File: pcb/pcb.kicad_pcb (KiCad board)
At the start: 2 copper layers, 61 x 81 mm, 46 parts, among them J1 LEFT, J2 LEFT-EXT, J3 RIGHT, J4 RIGHT-EXT, J5 EXT POWER, J6 RJ45, J7 RJ45, SW1 Reset, SW2 Factory Reset, SW3 User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

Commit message: :pencil: Initial pass at firmware and updates to the PCB.
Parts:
- added C13: 100nF, Capacitor_SMD:C_0603_1608Metric, F.Cu at (112.7, 108.1)
- D3: value CAN RX -> CAN TX
- D4: value CAN TX -> CAN RX
- moved JP1 15.1 mm to (159.7, 108.6), turned to 180 degrees
- moved J5 12.6 mm to (158.7, 120.0)
- moved U4 6.08 mm to (116.2, 110.3), turned to 90 degrees
- moved D4 3.42 mm to (111.2, 111.2), turned to 270 degrees
- moved R8 3.14 mm to (112.7, 111.2), turned to 90 degrees
- moved D3 2.68 mm to (111.2, 114.2), turned to 90 degrees
- moved R7 2.31 mm to (112.7, 114.2), turned to 270 degrees
- moved U2 2.02 mm to (140.9, 104.0)
- moved C1 1.89 mm to (145.6, 103.0)
- moved C11 1.78 mm to (117.3, 105.7)
- moved U5 1.70 mm to (122.7, 107.7)
- moved C12 1.70 mm to (128.3, 107.1)
- moved D5 1.17 mm to (117.6, 116.7)
- moved C3 1.12 mm to (136.5, 107.1)
- moved C4 1.12 mm to (133.5, 107.1)
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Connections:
- U4 pad 3: CAN-RX -> CAN-TX
- U4 pad 5: CAN-TX -> CAN-RX
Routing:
- net +3V3: track 187.0 -> 200.7 mm, vias 1 -> 6
- net VCC: track 24.0 -> 34.4 mm
- net Net-(R7-Pad1): track 13.4 -> 3.09 mm, vias 2 -> 0
- net VDDA: track 23.0 -> 32.9 mm
- net VDD: track 16.1 -> 8.95 mm
- net +5V: track 50.0 -> 43.3 mm, vias 0 -> 1
- net CAN-RX: track 58.1 -> 52.6 mm
- net CAN-H: track 38.3 -> 33.1 mm, vias 0 -> 1
- net CAN-TX: track 66.4 -> 61.6 mm
- net Net-(R8-Pad1): track 3.54 -> 6.74 mm
- net CAN-L: track 35.8 -> 33.7 mm, vias 0 -> 1
- net RESET: track 49.2 -> 47.4 mm
- net /5V-BST: track 1.55 -> 2.60 mm
- net Net-(C2-Pad1): track 8.61 -> 9.67 mm
- net ALT-B: track 19.1 -> 20.1 mm
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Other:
- board text added: "CAN"
- board text added: "Remove JP1 to use USB"
- board text added: "WARNING"
- board text added: "v1.0 Nov 2020"
- board text removed: "!WARNING!"
- board text removed: "CAN Activity"
- board text removed: "Remove JP1 when using USB"

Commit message: :pencil: Corrections to part numbers
* C2 should have been 100nF and not 22uF
* U3 needs to be able to provide 1A and not 600mA.
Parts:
- C2: value 22uF -> 100nF
- U3: value NCP1117 -> AP2114-3.3

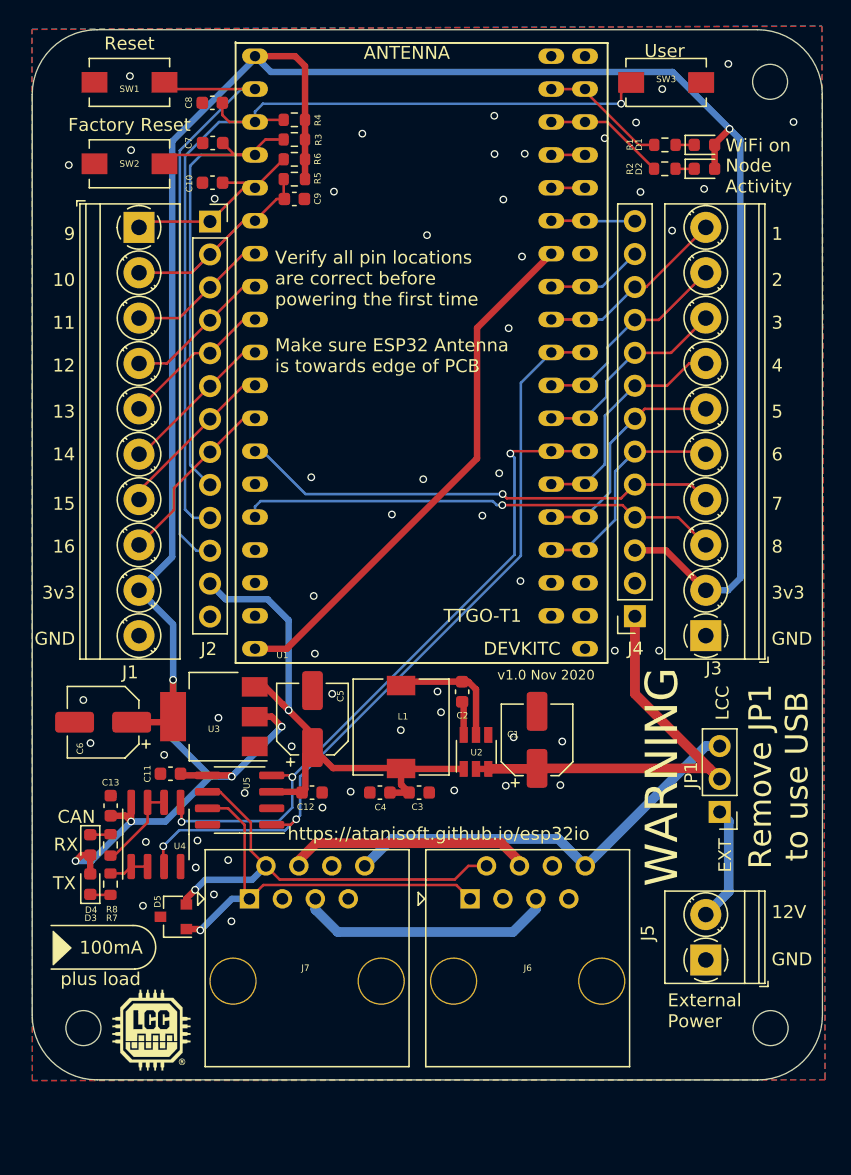
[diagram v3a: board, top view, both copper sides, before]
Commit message: :pencil: Add Fiducials to PCB :pencil: Adjust LED colors so they are not all red
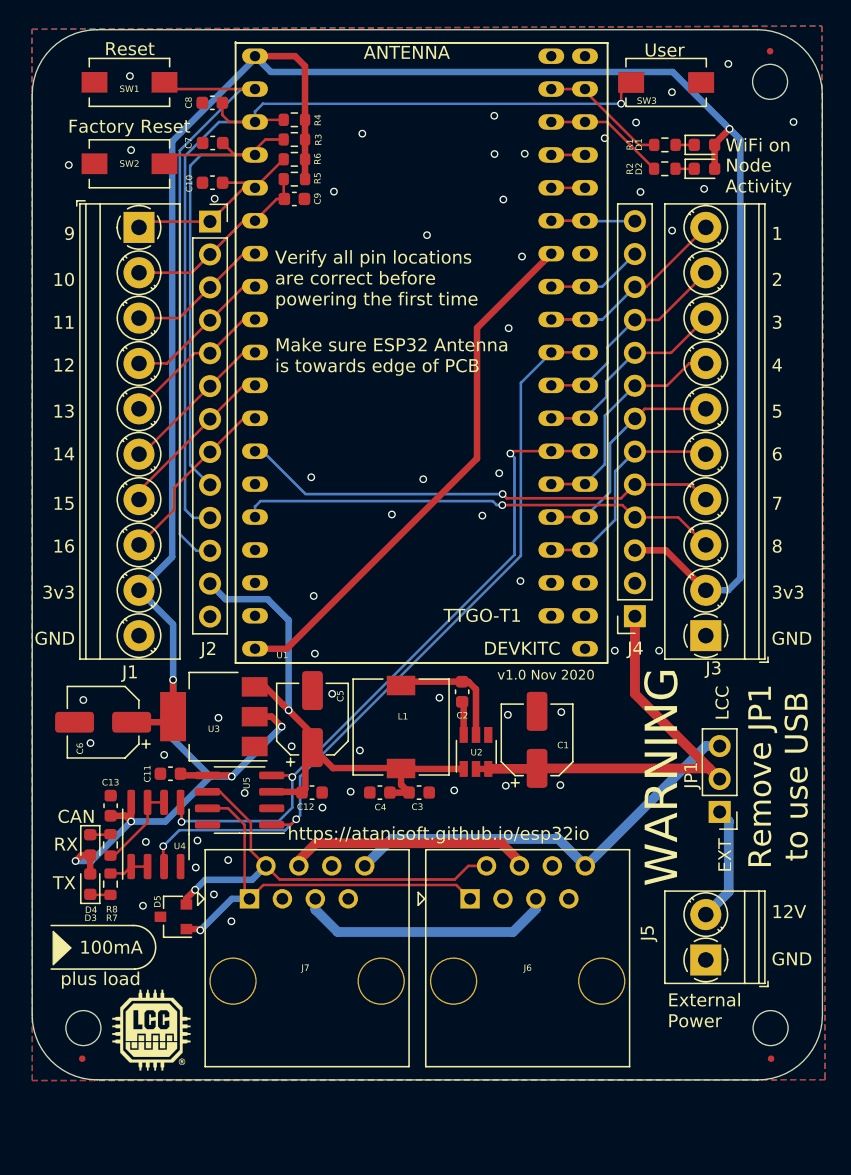
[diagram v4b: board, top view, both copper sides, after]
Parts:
- added FID1: Fiducial, Fiducial:Fiducial_0.5mm_Mask1mm, F.Cu at (163.6, 49.9)
- added FID2: Fiducial, Fiducial:Fiducial_0.5mm_Mask1mm, F.Cu at (110.5, 127.7)
- added FID3: Fiducial, Fiducial:Fiducial_0.5mm_Mask1mm, F.Cu at (163.7, 127.7)
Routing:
- net GND: vias 55 -> 54
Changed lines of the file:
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@@
     (thickness 1.6)
     (drawings 53)
-    (tracks 395)
+    (tracks 394)
     (zones 0)
-    (modules 47)
+    (modules 50)
     (nets 47)
   )
@@
   (title_block
     (title "ESP32 IO Board")
-    (date 2020-11-16)
+    (date 2020-11-19)
     (rev 1.0)
   )
@@
     (add_net VDDA)
     (add_net WIFI_LED)
+  )
+  (module Fiducial:Fiducial_0.5mm_Mask1mm (layer F.Cu)
+    (at 163.69 127.65)
+    (descr "Circular Fiducial, 0.5mm bare copper, 1mm soldermask opening (Level C)")
+    (tags fiducial)
+    (attr smd)
+    (fp_text reference FID3 (at 0 -1.5) (layer F.SilkS) hide
+      (effects (font (size 1 1) (thickness 0.15)))
+    )
+    (fp_text value Fiducial (at 0 1.5) (layer F.Fab)
+      (effects (font (size 1 1) (thickness 0.15)))
+    )
+    (fp_circle (center 0 0) (end 0.5 0) (layer F.Fab) (width 0.1))
+    (fp_circle (center 0 0) (end 0.75 0) (layer F.CrtYd) (width 0.05))
+    (fp_text user %R (at 0 0) (layer F.Fab)
+      (effects (font (size 0.2 0.2) (thickness 0.04)))
+    )
+    (pad "" smd circle (at 0 0) (size 0.5 0.5) (layers F.Cu F.Mask)
+      (solder_mask_margin 0.25) (clearance 0.25))
+  )
+  (module Fiducial:Fiducial_0.5mm_Mask1mm (layer F.Cu)
+    (at 110.54 127.65)
+    (descr "Circular Fiducial, 0.5mm bare copper, 1mm soldermask opening (Level C)")
+    (tags fiducial)
+    (attr smd)
+    (fp_text reference FID2 (at 0 -1.5) (layer F.SilkS) hide
+      (effects (font (size 1 1) (thickness 0.15)))
+    )
+    (fp_text value Fiducial (at 0 1.5) (layer F.Fab)
+      (effects (font (size 1 1) (thickness 0.15)))
+    )
+    (fp_circle (center 0 0) (end 0.5 0) (layer F.Fab) (width 0.1))
+    (fp_circle (center 0 0) (end 0.75 0) (layer F.CrtYd) (width 0.05))
+    (fp_text user %R (at 0 0) (layer F.Fab)
+      (effects (font (size 0.2 0.2) (thickness 0.04)))
+    )
+    (pad "" smd circle (at 0 0) (size 0.5 0.5) (layers F.Cu F.Mask)
+      (solder_mask_margin 0.25) (clearance 0.25))
+  )
+  (module Fiducial:Fiducial_0.5mm_Mask1mm (layer F.Cu)
+    (at 163.61 49.92)
+    (descr "Circular Fiducial, 0.5mm bare copper, 1mm soldermask opening (Level C)")
+    (tags fiducial)
+    (attr smd)
+    (fp_text reference FID1 (at 0 -1.5) (layer F.SilkS) hide
+      (effects (font (size 1 1) (thickness 0.15)))
+    )
+    (fp_text value Fiducial (at 0 1.5) (layer F.Fab)
+      (effects (font (size 1 1) (thickness 0.15)))
+    )
+    (fp_circle (center 0 0) (end 0.5 0) (layer F.Fab) (width 0.1))
+    (fp_circle (center 0 0) (end 0.75 0) (layer F.CrtYd) (width 0.05))
+    (fp_text user %R (at 0 0) (layer F.Fab)
+      (effects (font (size 0.2 0.2) (thickness 0.04)))
+    )
+    (pad "" smd circle (at 0 0) (size 0.5 0.5) (layers F.Cu F.Mask)
+      (solder_mask_margin 0.25) (clearance 0.25))
   )
   (module Connector_PinHeader_2.54mm:PinHeader_1x03_P2.54mm_Vertical (layer F.Cu)
@@
     (descr "Light Touch Switch, https://industrial.panasonic.com/cdbs/www-data/pdf/ATK0000/ATK0000CE7.pdf")
     (attr smd)
-    (fp_text reference SW3 (at 0 -0.254) (layer F.SilkS)
-      (effects (font (size 0.5 0.5) (thickness 0.1)))
-    )
-    (fp_text value User (at -0.12 -2.43) (layer F.SilkS)
+    (fp_text reference SW3 (at -1.49 1.42) (layer F.SilkS)
+      (effects (font (size 0.5 0.5) (thickness 0.1)))
+    )
+    (fp_text value User (at -0.13 -2.47) (layer F.SilkS)
       (effects (font (size 1 1) (thickness 0.15)))
     )
@@
       (effects (font (size 0.5 0.5) (thickness 0.1)))
     )
-    (fp_text value "Factory Reset" (at 0 3) (layer F.SilkS)
+    (fp_text value "Factory Reset" (at 0.012 2.864) (layer F.SilkS)
       (effects (font (size 1 1) (thickness 0.15)))
     )
@@
       (effects (font (size 0.5 0.5) (thickness 0.1)))
     )
-    (fp_text value Reset (at 0 3) (layer F.SilkS)
+    (fp_text value Reset (at -0.018 2.564) (layer F.SilkS)
       (effects (font (size 1 1) (thickness 0.15)))
     )
@@
     (tags "capacitor electrolytic")
     (attr smd)
-    (fp_text reference C1 (at 0.42 -1.85 180) (layer F.SilkS)
+    (fp_text reference C1 (at -0.42 2.01 180) (layer F.SilkS)
       (effects (font (size 0.5 0.5) (thickness 0.1)))
     )
@@
   (via (at 115.225 115.85) (size 0.6) (drill 0.4) (layers F.Cu B.Cu) (net 1))
   (via (at 122.05 117.05) (size 0.6) (drill 0.4) (layers F.Cu B.Cu) (net 1))
-  (via (at 155.29 52.84) (size 0.6) (drill 0.4) (layers F.Cu B.Cu) (net 1))
+  (via (at 156.04 53.08) (size 0.6) (drill 0.4) (layers F.Cu B.Cu) (net 1))
   (via (at 129.96 60.75) (size 0.6) (drill 0.4) (layers F.Cu B.Cu) (net 1))
   (via (at 109.5 58.7) (size 0.6) (drill 0.4) (layers F.Cu B.Cu) (net 1))
@@
   (via (at 128.21 82.79) (size 0.6) (drill 0.4) (layers F.Cu B.Cu) (net 1))
   (via (at 144.35 90.8) (size 0.6) (drill 0.4) (layers F.Cu B.Cu) (net 1))
-  (via (at 135.12 102.3) (size 0.6) (drill 0.4) (layers F.Cu B.Cu) (net 1))
+  (via (at 131.96 103.87) (size 0.6) (drill 0.4) (layers F.Cu B.Cu) (net 1))
   (via (at 158.52 60.54) (size 0.6) (drill 0.4) (layers F.Cu B.Cu) (net 1))
   (via (at 165.42 55.38) (size 0.6) (drill 0.4) (layers F.Cu B.Cu) (net 1))
@@
   (via (at 121.05 101.35) (size 0.6) (drill 0.4) (layers F.Cu B.Cu) (net 1))
   (via (at 111.175 103.3) (size 0.6) (drill 0.4) (layers F.Cu B.Cu) (net 1))
-  (via (at 147.575 103.175) (size 0.6) (drill 0.4) (layers F.Cu B.Cu) (net 1))
+  (via (at 147.5 100.91) (size 0.6) (drill 0.4) (layers F.Cu B.Cu) (net 1))
   (via (at 139.24 106.95) (size 0.6) (drill 0.4) (layers F.Cu B.Cu) (net 1))
   (via (at 129.825 99.5) (size 0.6) (drill 0.4) (layers F.Cu B.Cu) (net 1))
-  (via (at 138.22 100.92) (size 0.6) (drill 0.4) (layers F.Cu B.Cu) (net 1))
+  (via (at 138.1 99.8) (size 0.6) (drill 0.4) (layers F.Cu B.Cu) (net 1))
   (via (at 143.22 106.59) (size 0.6) (drill 0.4) (layers F.Cu B.Cu) (net 1))
-  (via (at 143.825 102.85) (size 0.6) (drill 0.4) (layers F.Cu B.Cu) (net 1))
+  (via (at 143.38 101.12) (size 0.6) (drill 0.4) (layers F.Cu B.Cu) (net 1))
   (via (at 110.625 99.975) (size 0.6) (drill 0.4) (layers F.Cu B.Cu) (net 1))
   (via (at 134.43 85.66) (size 0.6) (drill 0.4) (layers F.Cu B.Cu) (net 1))
@@
   (via (at 114.31 57.55) (size 0.6) (drill 0.4) (layers F.Cu B.Cu) (net 1))
   (via (at 120.76 61.3) (size 0.6) (drill 0.4) (layers F.Cu B.Cu) (net 1))
-  (via (at 137.95 99.32) (size 0.6) (drill 0.4) (layers F.Cu B.Cu) (net 1))
   (via (at 147.43 106.54) (size 0.6) (drill 0.4) (layers F.Cu B.Cu) (net 1))
   (via (at 131.25 107.05) (size 0.6) (drill 0.4) (layers F.Cu B.Cu) (net 1))

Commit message: pcb update for rename of repo
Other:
- board text added: "https://atanisoft.github.io/esp32olcbio"

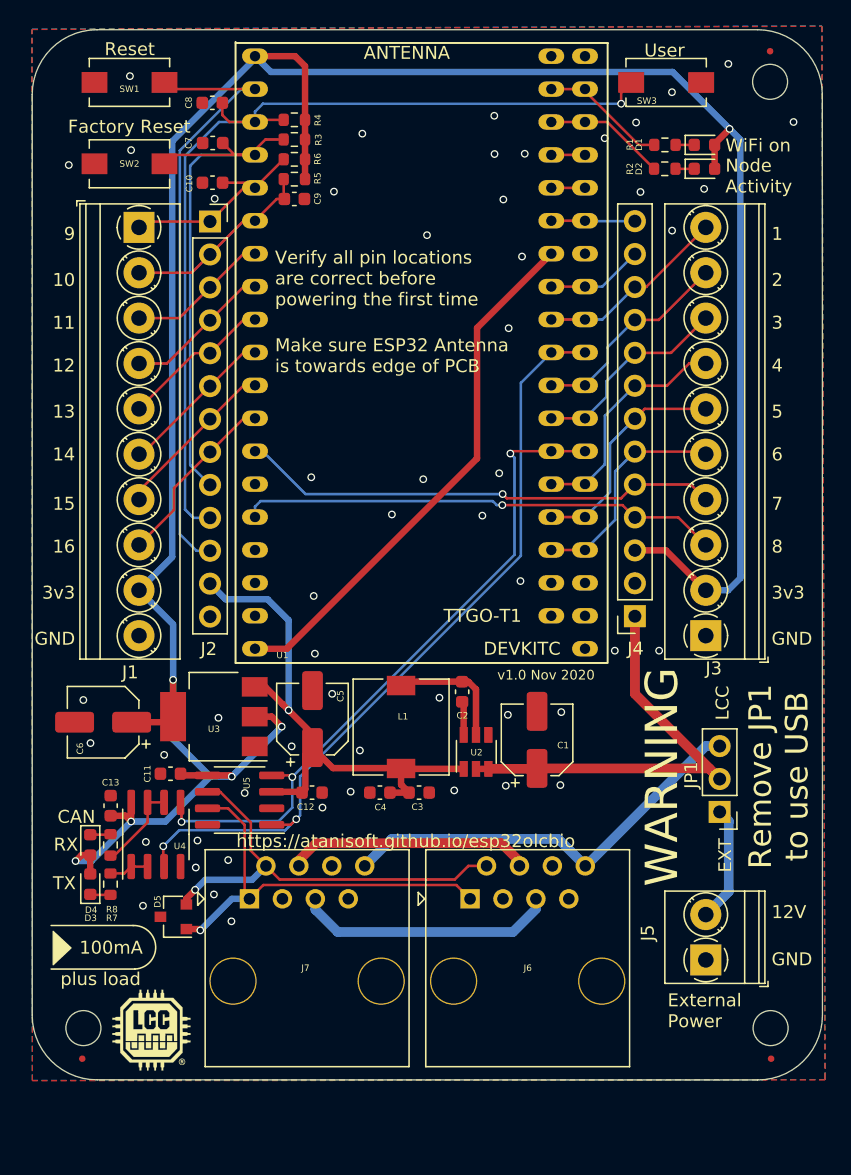
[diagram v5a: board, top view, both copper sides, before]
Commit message: PCB updates for KiCad6
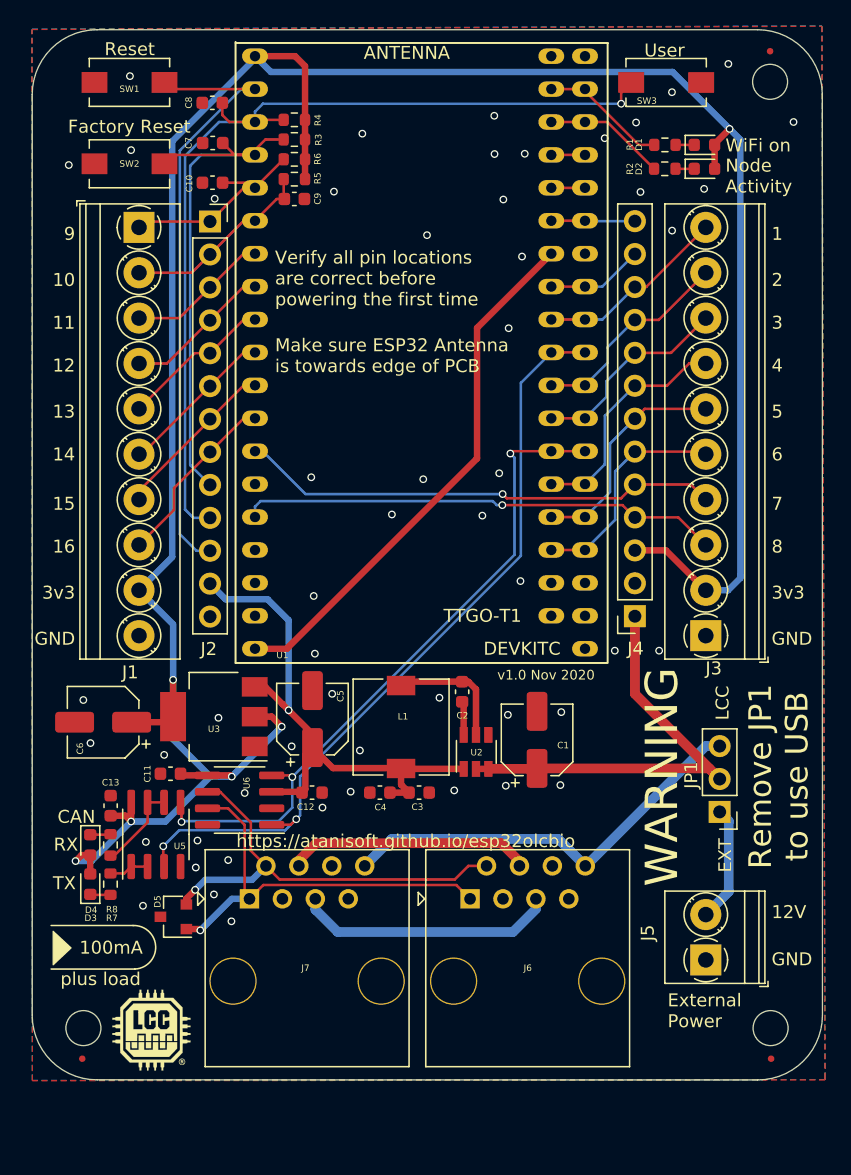
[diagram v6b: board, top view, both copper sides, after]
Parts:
- renumbered U4 to U5, U5 to U6
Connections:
- U1 pad 1: Net-(U1-Pad1) -> unconnected-(U1-Pad1)
- U1 pad 3: Net-(U1-Pad3) -> unconnected-(U1-Pad3)
- U1 pad 5V: Net-(U1-Pad5V) -> unconnected-(U1-Pad5V)
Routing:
- net unconnected-(U1-Pad5V): track 0.00 -> 41.4 mm
- net Net-(U1-Pad5V): track 41.4 -> 0.00 mm
- net unconnected-(U1-Pad3): track 0.00 -> 2.60 mm
- net unconnected-(U1-Pad1): track 0.00 -> 2.60 mm
- net Net-(U1-Pad3): track 2.60 -> 0.00 mm
- net Net-(U1-Pad1): track 2.60 -> 0.00 mm
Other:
- net class Default removed

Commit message: IO PCB v1.1
Spaced out RJ45 jacks to provide easier access to USB connector.

Fixes: https://github.com/atanisoft/Esp32OlcbIO/issues/3
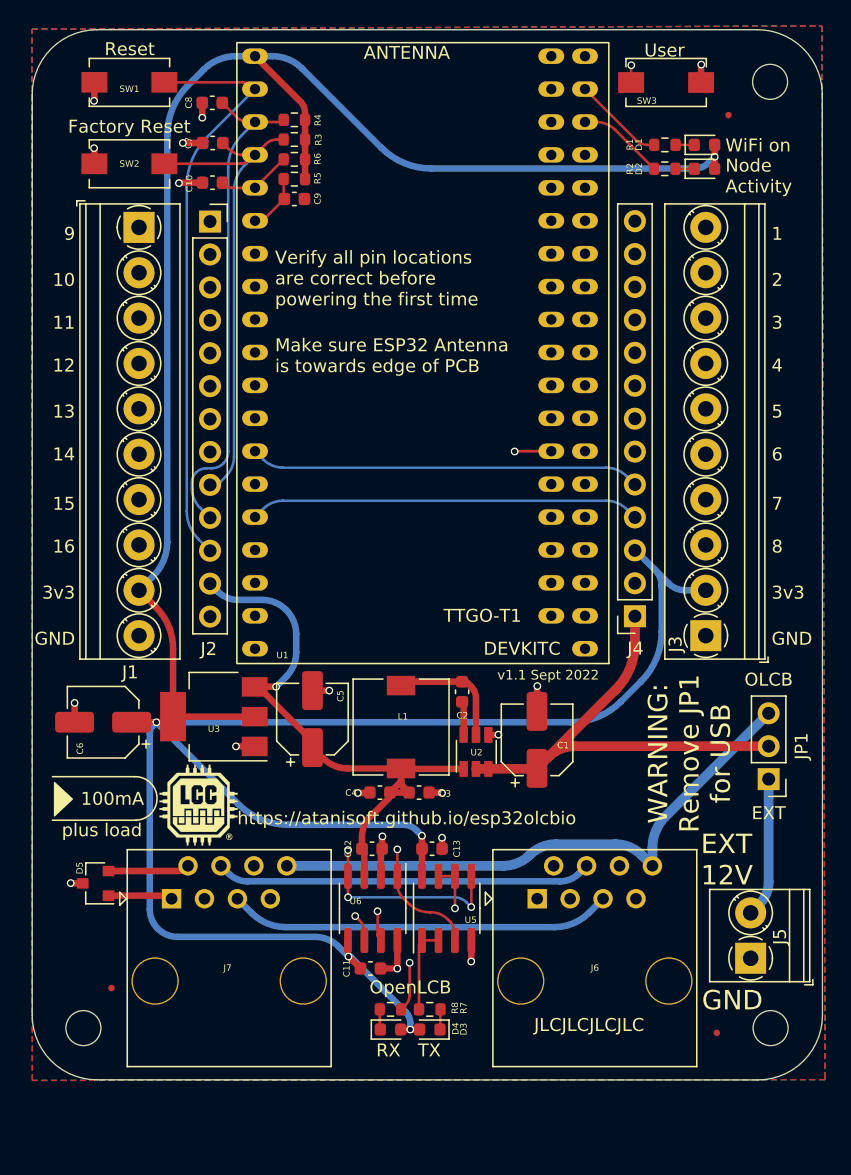
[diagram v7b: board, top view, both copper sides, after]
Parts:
- added REF**: OSHW-Logo2_7.3x6mm_SilkScreen, Symbol:OSHW-Logo2_7.3x6mm_SilkScreen, B.Cu at (136.9, 64.8)
- added REF**: KiCad-Logo2_5mm_SilkScreen, Symbol:KiCad-Logo2_5mm_SilkScreen, B.Cu at (137.0, 58.6)
- moved D3 28.5 mm to (137.4, 125.4), turned to 180 degrees
- moved D4 27.2 mm to (134.3, 125.4), turned to 0 degrees
- moved R7 26.5 mm to (137.4, 123.8), turned to 0 degrees
- moved R8 25.1 mm to (134.3, 123.8), turned to 180 degrees
- moved C13 25.0 mm to (137.5, 111.5), turned to 180 degrees
- moved U5 23.2 mm to (138.7, 116.0)
- moved C11 21.5 mm to (132.8, 120.7), turned to 0 degrees
- moved G*** 17.7 mm to (119.5, 108.0)
- moved U6 13.2 mm to (132.9, 116.0), turned to -90 degrees
- moved D5 6.54 mm to (111.6, 114.1)
- moved C12 6.34 mm to (132.9, 111.5)
- moved J7 6.01 mm to (117.4, 115.3)
- moved FID2 5.90 mm to (112.8, 122.2)
- moved FID1 5.88 mm to (160.4, 54.9)
- moved J6 5.18 mm to (145.6, 115.3)
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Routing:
- net +3V3: track 200.7 -> 243.9 mm, vias 6 -> 5
- net unconnected-(U1-Pad5V): track 41.4 -> 0.00 mm
- net GND: track 0.00 -> 27.5 mm, vias 54 -> 18
- net VDDA: track 32.9 -> 44.5 mm
- net ALT-A: track 18.9 -> 29.0 mm
- net ALT-B: track 20.1 -> 29.7 mm
- net CAN-L: track 33.7 -> 41.5 mm
- net CAN-TX: track 61.6 -> 54.8 mm, vias 2 -> 1
- net Net-(R8-Pad1): track 6.74 -> 13.2 mm, vias 0 -> 2
- net CAN-RX: track 52.6 -> 57.0 mm, vias 3 -> 4
- net CAN-H: track 33.1 -> 37.3 mm
- net FACTORY_RESET: track 43.7 -> 39.6 mm
- net Net-(R7-Pad1): track 3.09 -> 6.65 mm
- net VCC: track 34.4 -> 37.7 mm
- net +5V: track 43.3 -> 46.1 mm
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- added copper zone on In1.Cu, net GND
- added copper zone on In2.Cu, net GND
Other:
- copper layers 2 -> 4
- board text added: "EXT 12V"
- board text added: "OLCB"
- board text added: "OpenLCB"
- board text added: "WARNING: Remove JP1 for USB"
- board text added: "v1.1 Sept 2022"
- board text added: "v1.1 September 2022"
- board text removed: "12V"
- board text removed: "CAN"
- board text removed: "External Power"
- board text removed: "LCC"
- board text removed: "Remove JP1 to use USB"
- board text removed: "WARNING"
- board text removed: "v1.0 Nov 2020"
- board text removed: "v1.0 November 2020"
